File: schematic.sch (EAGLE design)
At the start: 21 parts, among them IC1 TPS6300, J1 FTDI_DEVICE, U1 ATMEGA328P_TQFP, U2 GY-521MPU6050

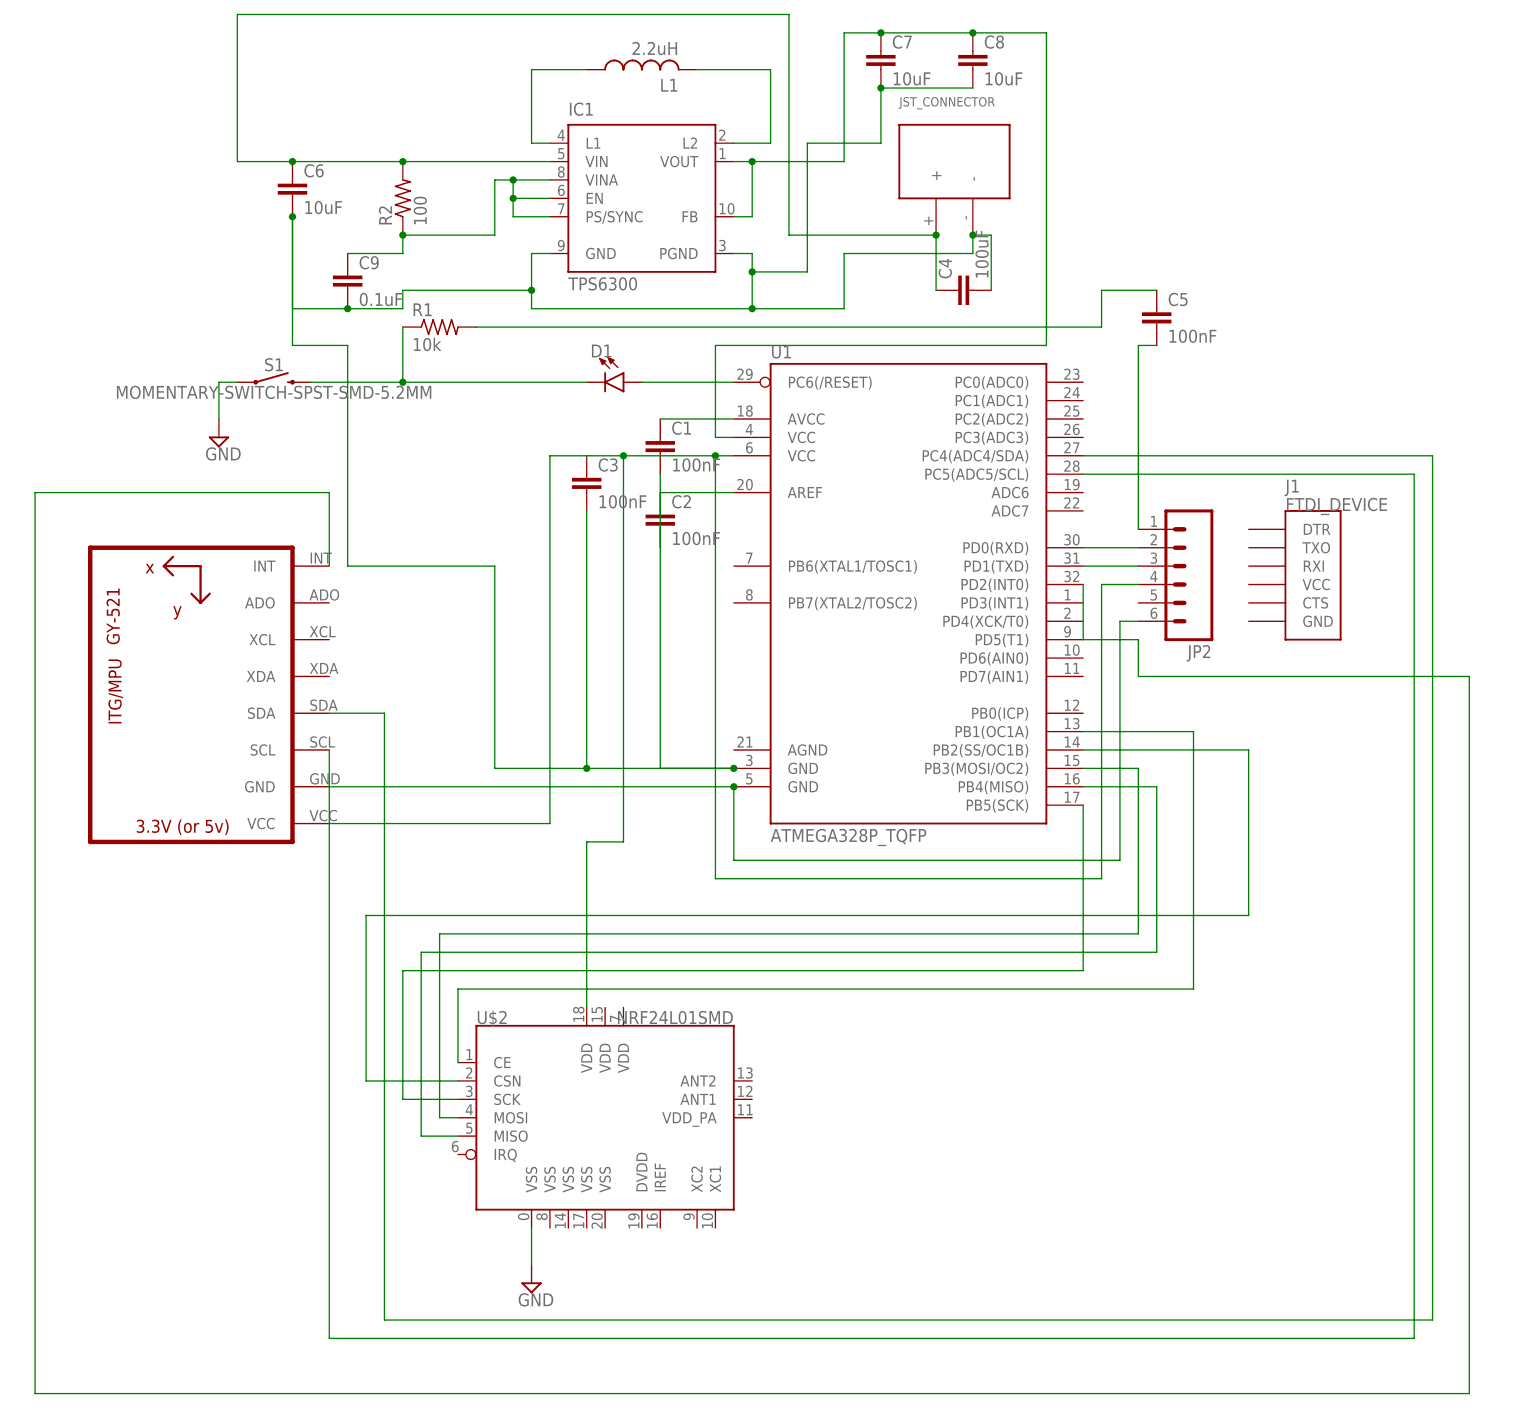
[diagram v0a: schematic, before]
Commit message: Updated schematic. TODO: voltage divider, voltage regulator, motor driver, battery
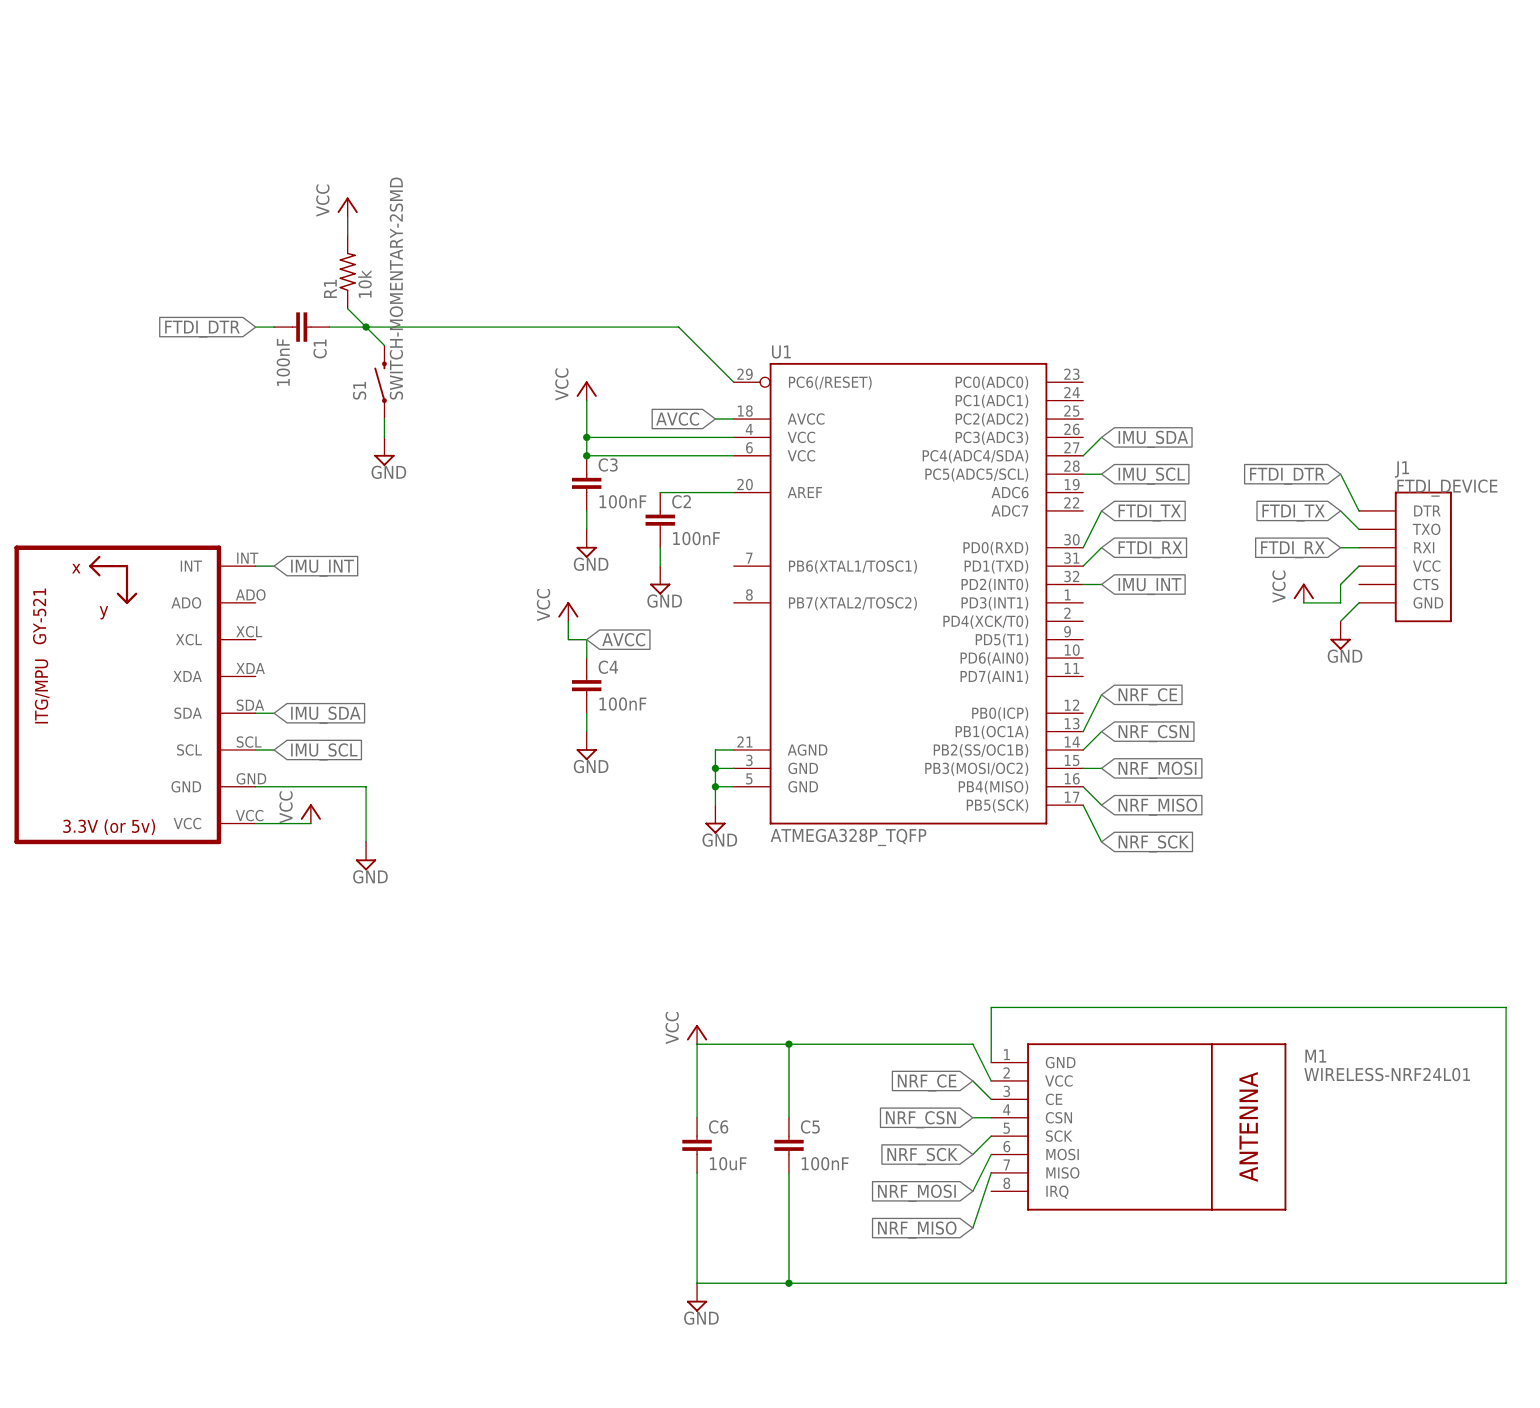
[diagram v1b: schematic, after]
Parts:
- removed C7, C8: 10uF, rcl:C-EUC0603
- removed C9: 0.1uF, rcl:C-EUC0603
- removed D1: (no value), SparkFun-LED:LED0603
- removed IC1: TPS6300, texas:TPS6300
- removed JP2: (no value), SparkFun:M06SMD-FEMALE-V2
- removed L1: 2.2uH, rcl:L-US0204/5
- removed R2: 100, rcl:R-US_R0603
- removed U$1: JST_CONNECTOR_FEMALE, quad:JST_CONNECTOR_FEMALE
- removed U$2: NRF24L01SMD, SparkFun-RF:NRF24L01SMD
- added M1: WIRELESS-NRF24L01, quad:WIRELESS-NRF24L01
- C4: value 100uF -> 100nF; device rcl:C-EUC2220K -> rcl:C-EUC0603
- R1: device resistor:R-US_R0603 -> rcl:R-US_R0603
- S1: value MOMENTARY-SWITCH-SPST-SMD-5.2MM -> SWITCH-MOMENTARY-2SMD; device SparkFun-Switches:MOMENTARY-SWITCH-SPST-SMD-5.2MM -> quad:SWITCH-MOMENTARY-2SMD
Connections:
- net N$17 renamed IMU_SCL
- net N$18 renamed IMU_SDA
- net N$19 renamed IMU_INT
- removed net N$10: C5.2, JP2.1
- removed net N$11: C5.1, R1.2
- removed net N$12: D1.A, U1.PC6(/RESET)
- removed net N$13: D1.C, R1.1, S1.2
- removed net N$14: U$2.MOSI, U1.PB3(MOSI/OC2)
- removed net N$15: U$2.MISO, U1.PB4(MISO)
- removed net N$16: C3.1, JP2.4, U$2.VDD@18, U1.VCC@6, U2.VCC
- removed net N$20: U$2.SCK, U1.PB5(SCK)
- removed net N$21: U$2.CE, U1.PB1(OC1A)
- removed net N$22: U$2.CSN, U1.PB2(SS/OC1B)
- removed net N$23: IC1G$1.L1, L1.1
- removed net N$24: IC1G$1.L2, L1.2
- removed net N$25: C7.1, C8.1, IC1G$1.FB, IC1G$1.VOUT, U1.VCC@4
- removed net N$28: C9.1, IC1G$1.EN, IC1G$1.PS/SYNC, IC1G$1.VINA, R2.1
- removed net N$3: JP2.2, U1.PD0(RXD)
- removed net N$6: C4.1, C6.1, IC1G$1.VIN, R2.2, U$1.+
- removed net N$7: C1.2, C2.2, C3.2, C4.2, C6.2, C7.2, C8.2, C9.2, IC1G$1.GND, IC1G$1.PGND, U$1.-, U1.GND@3
- removed net N$9: JP2.6, U1.GND@5, U2.GND
- new net AVCC: C4.1, U1.AVCC
- new net FTDI_DTR: C1.2, J1.DTR
- new net FTDI_RX: J1.RXI, U1.PD1(TXD)
- new net FTDI_TX: J1.TXO, U1.PD0(RXD)
- new net NRF_CE: M1.CE, U1.PB1(OC1A)
- new net NRF_CSN: M1.CSN, U1.PB2(SS/OC1B)
- new net NRF_MISO: M1.MISO, U1.PB4(MISO)
- new net NRF_MOSI: M1.MOSI, U1.PB3(MOSI/OC2)
- new net NRF_SCK: M1.SCK, U1.PB5(SCK)
- new net VCC: C3.1, C5.1, C6.1, J1.VCC, M1.VCC, R1.2, U1.VCC@4, U1.VCC@6, U2.VCC
- net GND: now also C2.2, C3.2, J1.GND, U1.AGND, U1.GND@3, U1.GND@5, U2.GND; no longer U$2.VSS@0
- net N$1: now also R1.1, S1.2; no longer U1.AVCC
- net N$4: now also C5.2, C6.2, M1.GND; no longer JP2.3, U1.PD1(TXD)
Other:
- moved on the sheet: C1, C4, C5, C6, J1, R1, S1
